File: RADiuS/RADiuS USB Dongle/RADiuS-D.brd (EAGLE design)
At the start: 22.9 x 57.2 mm, 13 parts

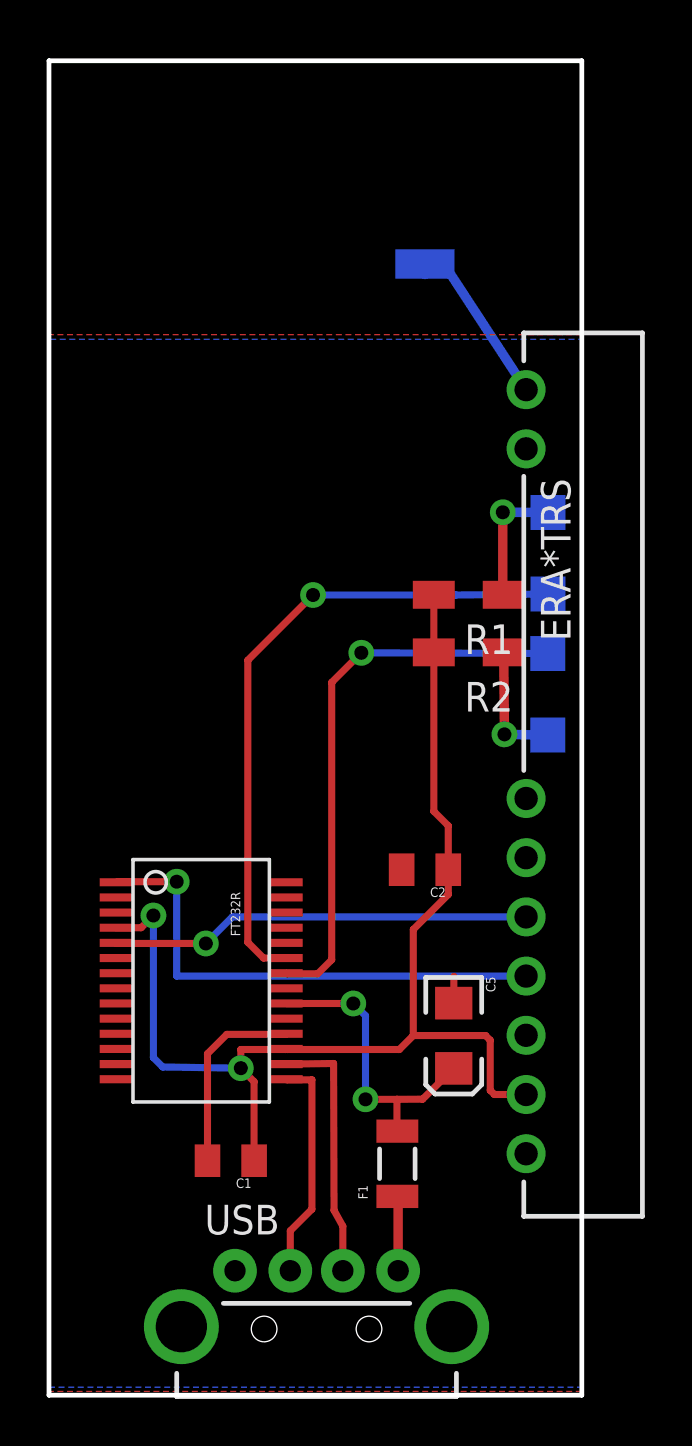
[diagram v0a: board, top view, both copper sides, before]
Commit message: RADiuS USB Dongle revisions
Moved USB connector to the other side of the board, trace changes, skinnified the board, and added logos/text.
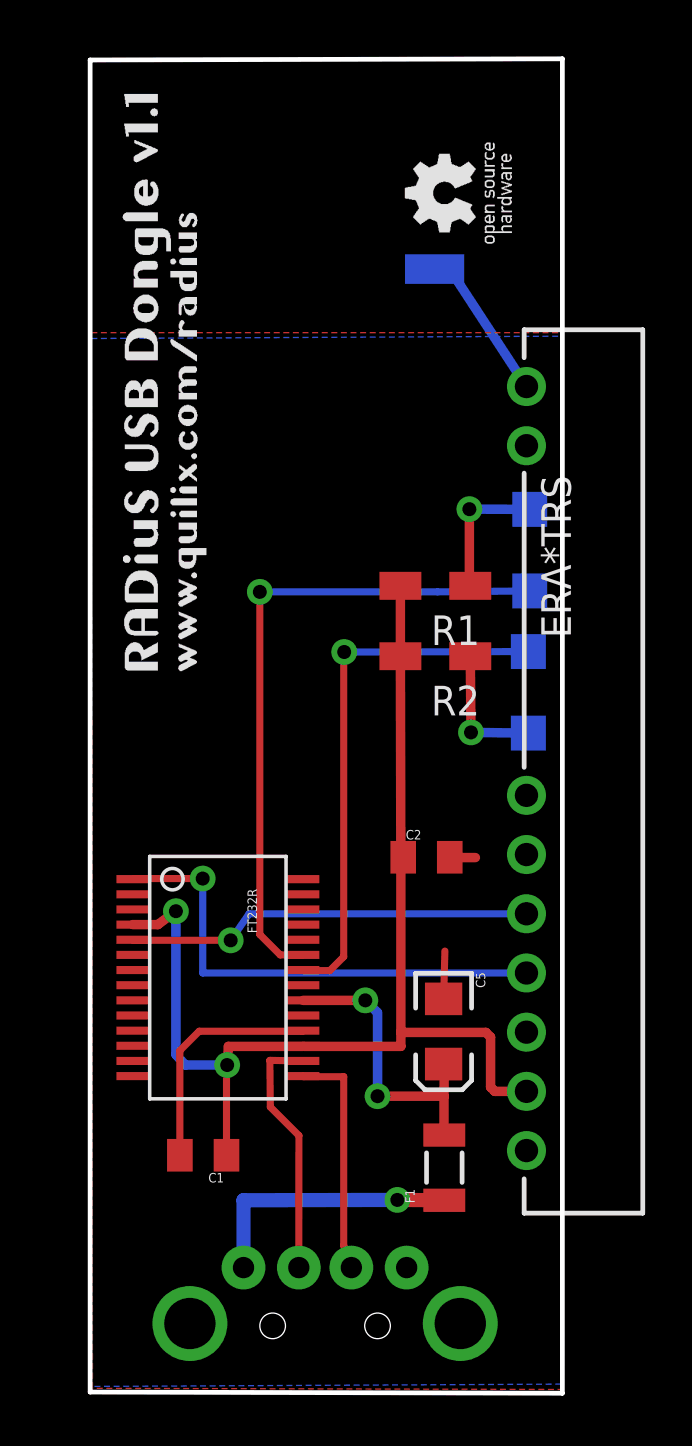
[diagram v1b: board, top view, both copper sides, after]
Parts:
- moved F1 2.02 mm to (17.4, 10.1)
- moved R1 1.49 mm to (17.0, 35.1)
- moved R2 1.44 mm to (17.0, 32.1)
- moved C1 1.21 mm to (7.09, 10.7)
- moved LED2 0.84 mm to (21.0, 30.5)
- moved LED1 0.80 mm to (21.1, 36.6)
- moved FT232R 0.73 mm to (7.72, 18.3)
- moved C2 0.54 mm to (16.7, 23.4), turned to 0 degrees
- moved C5 0.47 mm to (17.4, 16.0)
- moved ANT 0.47 mm to (17.0, 48.7)
- moved USB 0.39 mm to (12.3, 3.44), flipped to the bottom
- moved U$1 0.14 mm to (-0.01, 0.14)
- moved ERA*TRS 0.14 mm to (18.4, 27.1)
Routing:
- net N$3: track 3.20 -> 11.5 mm, vias 0 -> 1
- net GND: track 9.48 -> 13.1 mm
- net 3.3V: track 51.4 -> 50.3 mm
- net RXLED: track 23.9 -> 23.0 mm
- net TXD: track 21.7 -> 21.0 mm
- net RXD: track 18.1 -> 17.5 mm
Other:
- board size 22.9 x 57.2 mm -> 20.3 x 57.2 mm

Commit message: production update for RADiuS projects
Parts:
- removed U$1: CREATIVE_COMMONS, SparkFun:CREATIVE_COMMONS
- moved ERA*TRS 3.61 mm to (22.0, 27.6), flipped to the bottom
- moved R1 1.62 mm to (15.5, 35.6)
- moved R2 1.62 mm to (15.5, 32.5)
- moved C2 1.62 mm to (15.1, 23.9)
- moved C5 1.62 mm to (15.9, 16.4)
- moved ANT 1.62 mm to (15.5, 49.2)
- moved C1 1.62 mm to (5.54, 11.1)
- moved FT232R 1.62 mm to (6.17, 18.8)
- moved LED1 1.62 mm to (19.5, 37.1)
- moved USB 1.62 mm to (10.8, 3.92)
- moved F1 1.62 mm to (15.9, 10.6)
- moved LED2 1.62 mm to (19.5, 31.0)
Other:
- outline, holes or cut-outs redrawn
